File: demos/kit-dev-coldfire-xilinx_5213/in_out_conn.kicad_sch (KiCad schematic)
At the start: 73 parts, among them J201 JACK_2P, SW201 SW_PUSH, SW202 SW_PUSH, U201 74HC125, U202 MAX202, U203 MAX202, U204 MAX202, U205 PCA82C251

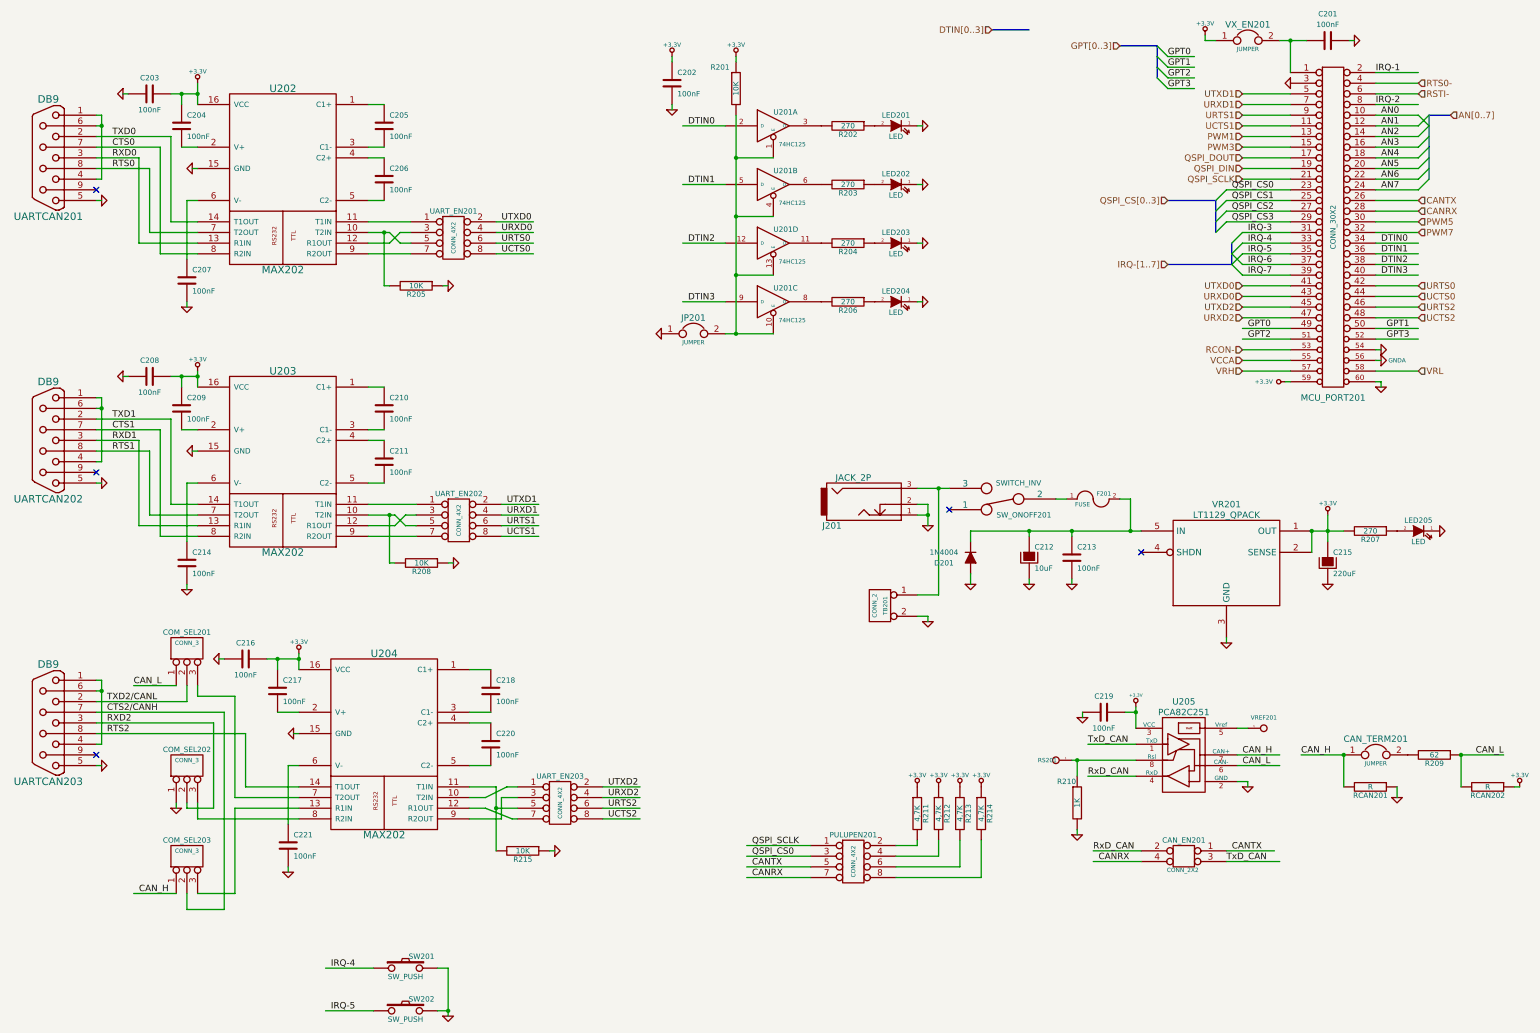
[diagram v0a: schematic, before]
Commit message: feat: update kicad to 9.0.0+dfsg-1
Signed-off-by: lhdjply <lhdjply@126.com>
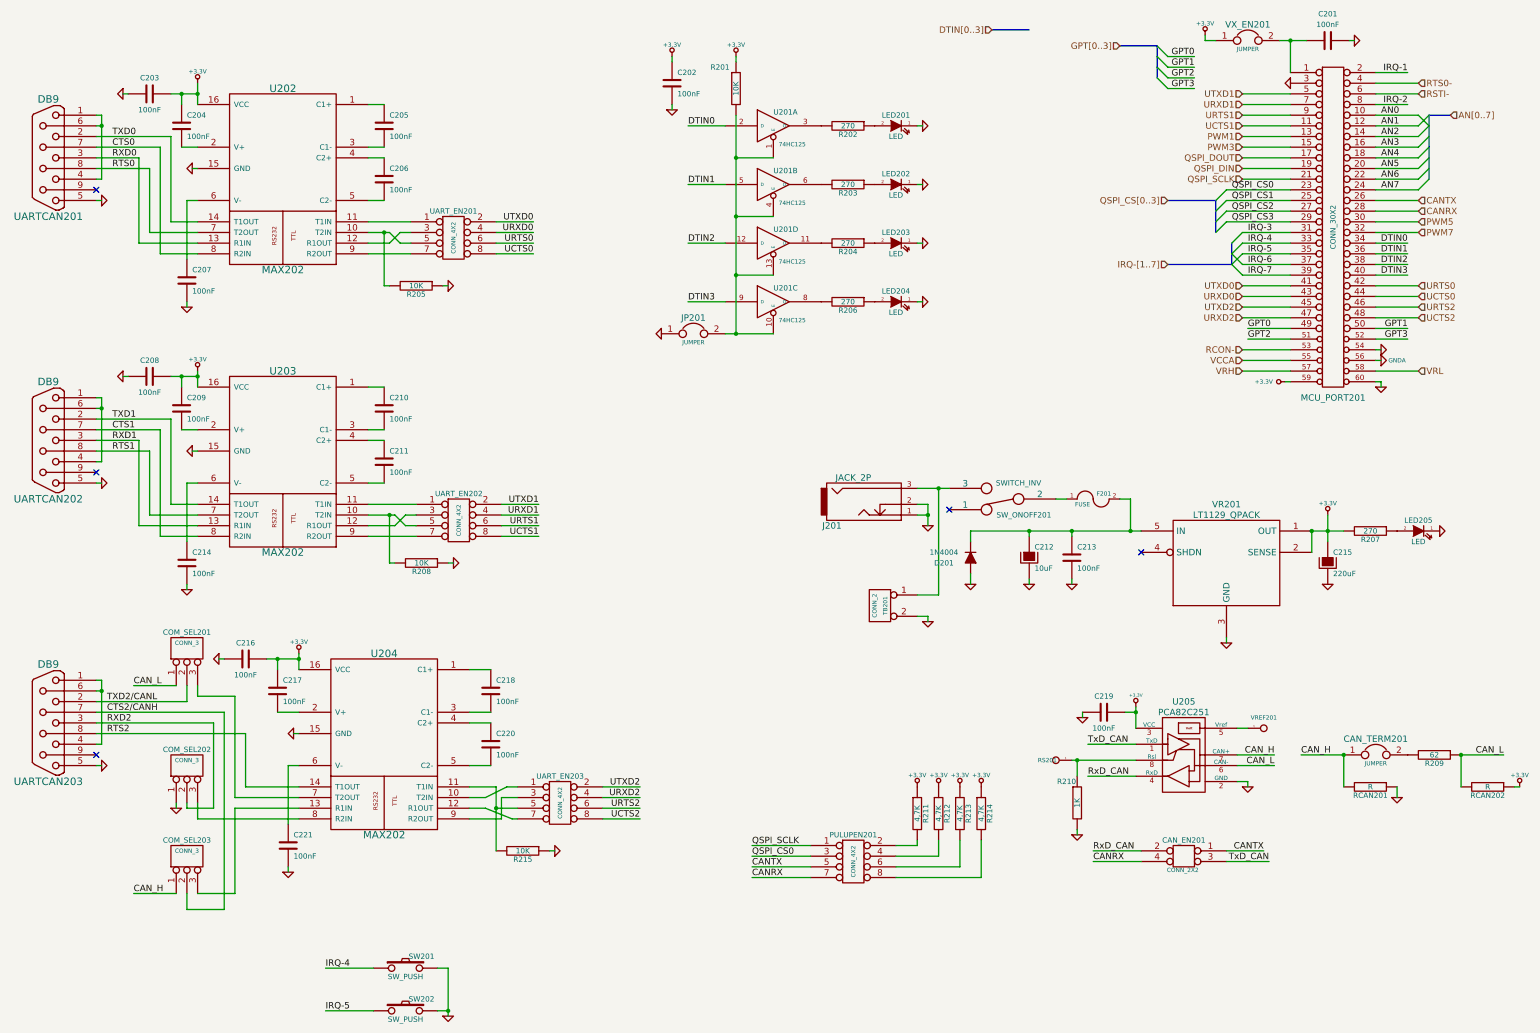
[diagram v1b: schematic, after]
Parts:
- C201, C202, C203, C204, C205, C206, C207, C208, C209, C210, C211, C213, C214, C216, C217, C218, C219, C220, C221: symbol kit-coldfire_schlib:C -> kit-dev-coldfire-xilinx_5213:C
- C212, C215: symbol kit-coldfire_schlib:CP -> kit-dev-coldfire-xilinx_5213:CP
- CAN_EN201: symbol kit-coldfire_schlib:CONN_2X2 -> kit-dev-coldfire-xilinx_5213:CONN_2X2
- CAN_TERM201, JP201, VX_EN201: symbol kit-coldfire_schlib:JUMPER -> kit-dev-coldfire-xilinx_5213:JUMPER
- COM_SEL201, COM_SEL202, COM_SEL203: symbol kit-coldfire_schlib:CONN_3 -> kit-dev-coldfire-xilinx_5213:CONN_3
- D201: symbol kit-coldfire_schlib:DIODE -> kit-dev-coldfire-xilinx_5213:DIODE
- F201: symbol kit-coldfire_schlib:FUSE -> kit-dev-coldfire-xilinx_5213:FUSE
- J201: symbol kit-coldfire_schlib:JACK_2P -> kit-dev-coldfire-xilinx_5213:JACK_2P
- LED201, LED202, LED203, LED204, LED205: symbol kit-coldfire_schlib:LED -> kit-dev-coldfire-xilinx_5213:LED
- MCU_PORT201: symbol kit-coldfire_schlib:CONN_30X2 -> kit-dev-coldfire-xilinx_5213:CONN_30X2
- PULUPEN201, UART_EN201, UART_EN202, UART_EN203: symbol kit-coldfire_schlib:CONN_4X2 -> kit-dev-coldfire-xilinx_5213:CONN_4X2
- R201, R202, R203, R204, R205, R206, R207, R208, R209, R210, R211, R212, R213, R214, R215, RCAN201, RCAN202: symbol kit-coldfire_schlib:R -> kit-dev-coldfire-xilinx_5213:R
- RS201, VREF201: symbol kit-coldfire_schlib:CONN_1 -> kit-dev-coldfire-xilinx_5213:CONN_1
- SW201, SW202: symbol kit-coldfire_schlib:SW_PUSH -> kit-dev-coldfire-xilinx_5213:SW_PUSH
- SW_ONOFF201: symbol kit-coldfire_schlib:SWITCH_INV -> kit-dev-coldfire-xilinx_5213:SWITCH_INV
- TB201: symbol kit-coldfire_schlib:CONN_2 -> kit-dev-coldfire-xilinx_5213:CONN_2
- U201: symbol kit-coldfire_schlib:74LS125 -> kit-dev-coldfire-xilinx_5213:74LS125
- U202, U203, U204: symbol kit-coldfire_schlib:MAX202 -> kit-dev-coldfire-xilinx_5213:MAX202
- U205: symbol kit-coldfire_schlib:PCA82C251 -> kit-dev-coldfire-xilinx_5213:PCA82C251
- UARTCAN201, UARTCAN202, UARTCAN203: symbol kit-coldfire_schlib:DB9 -> kit-dev-coldfire-xilinx_5213:DB9
- VR201: symbol kit-coldfire_schlib:LT1129_QPACK -> kit-dev-coldfire-xilinx_5213:LT1129_QPACK
